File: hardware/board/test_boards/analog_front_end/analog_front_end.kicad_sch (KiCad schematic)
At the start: 13 parts, among them J1 Conn_01x20_Female, J2 Conn_01x20_Female, U6 LM27762

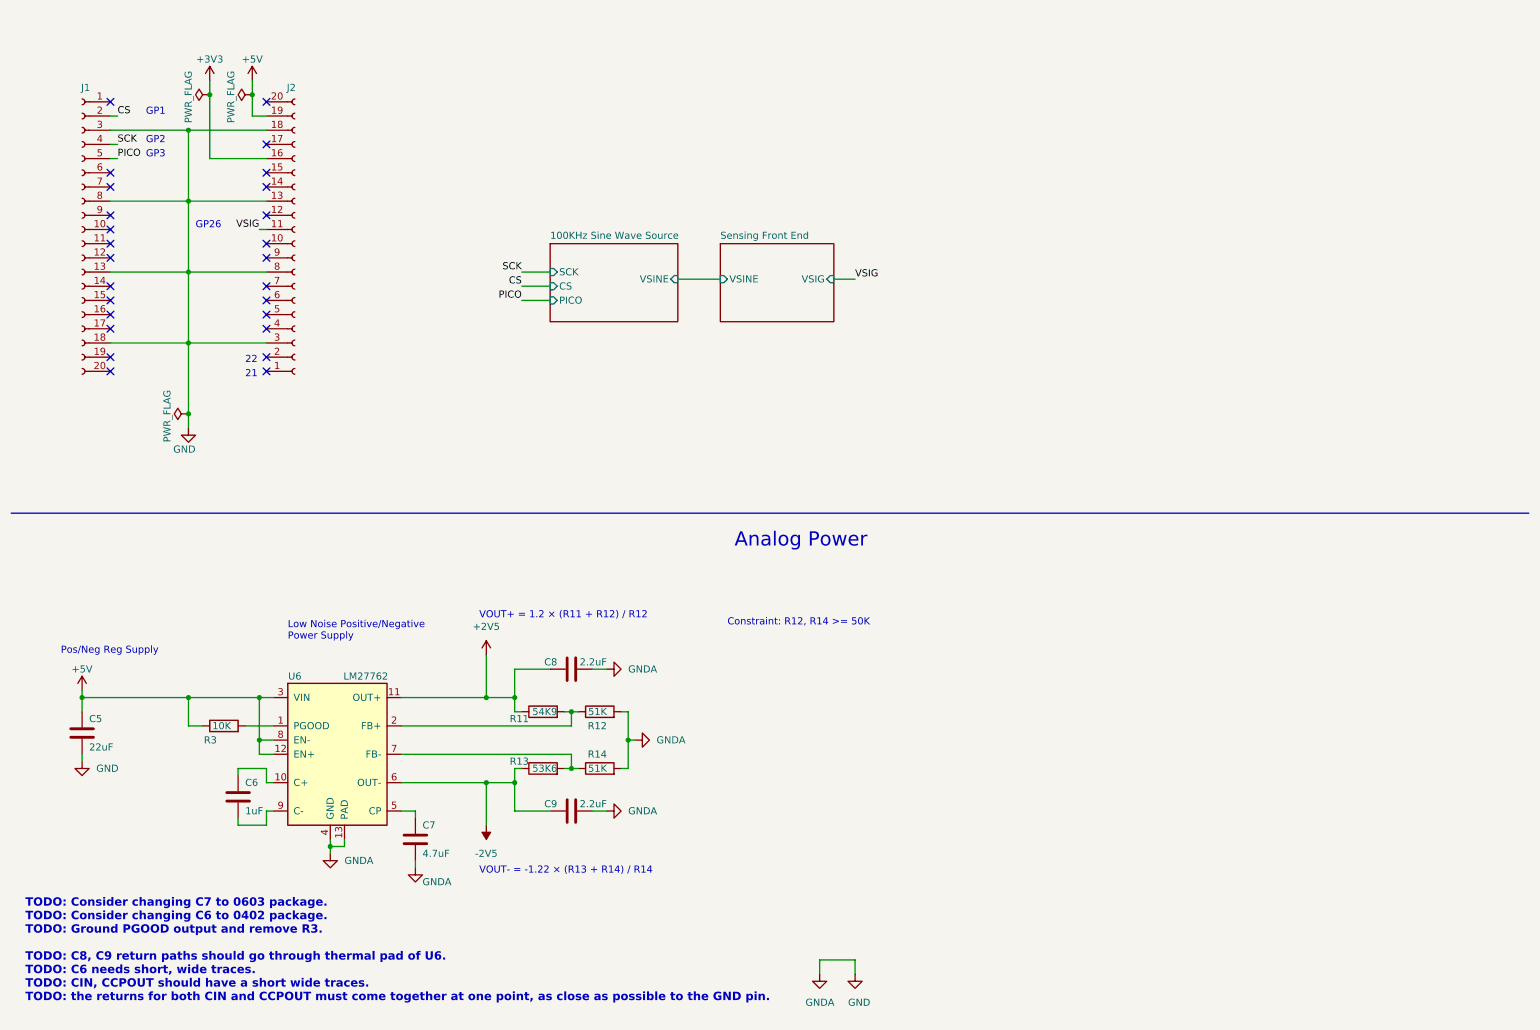
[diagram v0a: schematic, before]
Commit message: pcb rev3 with pcb guard and cable shield guard option
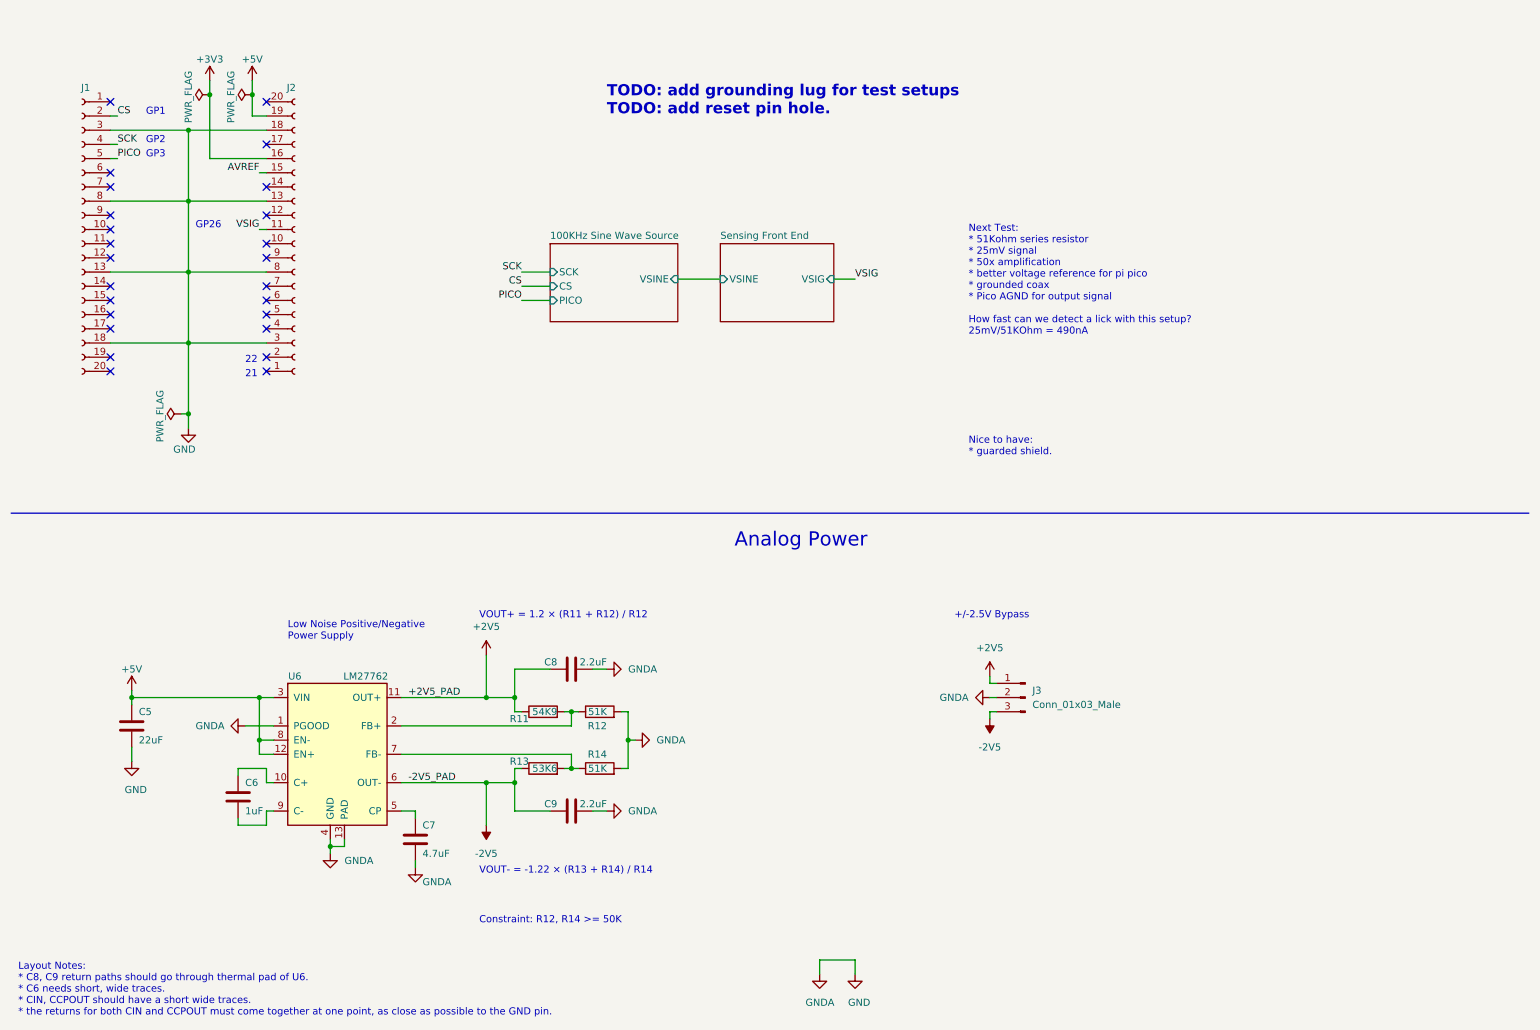
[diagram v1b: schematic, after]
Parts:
- removed R3: 10K, Resistor_SMD:R_0402_1005Metric_Pad0.72x0.64mm_HandSolder, symbol Device:R
- added J3: Conn_01x03_Male, Connector_PinHeader_2.54mm:PinHeader_1x03_P2.54mm_Vertical, symbol Connector:Conn_01x03_Male
- C6: footprint Capacitor_SMD:C_0603_1608Metric_Pad1.08x0.95mm_HandSolder -> Capacitor_SMD:C_0402_1005Metric_Pad0.74x0.62mm_HandSolder; Link https://www.digikey.com/en/products/detail/samsung-electro-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 -> https://www.digikey.com/en/products/detail/murata-electroni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; Manufacturer Samsung Electro-Mechanics -> Murata Electronics; Manufacturer Number CL10B105KA8NNNC -> GRM155R6YA105KE11J; Rated Voltage 25V -> 35V; Temperature Coefficient X7R -> X5R
- C7: footprint Capacitor_SMD:C_0805_2012Metric_Pad1.18x1.45mm_HandSolder -> Capacitor_SMD:C_0603_1608Metric_Pad1.08x0.95mm_HandSolder; Link https://www.digikey.com/en/products/detail/murata-electroni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 -> https://www.digikey.com/en/products/detail/samsung-electro-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; Manufacturer Murata Electronics -> Samsung Electro-Mechanics; Manufacturer Number GRM21BZ71H475KE15K -> CL10A475MA8NQNC; Rated Voltage 50V -> 25V; Temperature Coefficient X7R -> X5R; Tolerance 10% -> 20%
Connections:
- net +2V5: now also J3.1 (Pin_1)
- net -2V5: now also J3.3 (Pin_3)
- net GND: now also U6.1 (PGOOD), J3.2 (Pin_2)
- net AVREF: now reaches J2.15 (Pin_15)
- no-connect marks 26 -> 25
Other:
- note added: "+/-2.5V Bypass"
- note added: "Layout Notes: * C8, C9 return paths should go through thermal pad of U6. * C6 needs short, wide traces. * CIN, CCPOUT should have a short wide traces. * the returns for both CIN and CCPOUT must come together at one point, as close as possible to the GND pin."
- note added: "Next Test: * 51Kohm series resistor * 25mV signal * 50x amplification * better voltage reference for pi pico * grounded coax * Pico AGND for output signal How fast can we detect a lick with this setup? 25mV/51KOhm = 490nA"
- note added: "Nice to have: * guarded shield."
- note added: "TODO: add grounding lug for test setups TODO: add reset pin hole."
- note removed: "Pos/Neg Reg Supply"
- note removed: "TODO: Consider changing C7 to 0603 package. TODO: Consider changing C6 to 0402 package. TODO: Ground PGOOD output and remove R3. TODO: C8, C9 return paths should go through thermal pad of U6. TODO: C6 needs short, wide traces. TODO: CIN, CCPOUT should have a short wide traces. TODO: the returns for both CIN and CCPOUT must come together at one point, as close as possible to the GND pin."
- moved on the sheet: C5

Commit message: add design notes
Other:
- note added: "Next Test: * 50Kohm series resistor (or 100K) * 25mV signal * 50x amplification * better voltage reference for pi pico * grounded coax * Pico AGND for output signal How fast can we detect a lick with this setup? 25mV/51KOhm = 490nA 25mV/100KOhm = 250nA"
- note removed: "Next Test: * 51Kohm series resistor * 25mV signal * 50x amplification * better voltage reference for pi pico * grounded coax * Pico AGND for output signal How fast can we detect a lick with this setup? 25mV/51KOhm = 490nA"
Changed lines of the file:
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@@
     (effects (font (size 1.27 1.27)) (justify left bottom))
   )
-  (text "Next Test:\n* 51Kohm series resistor\n* 25mV signal\n* 50x amplification\n* better voltage reference for pi pico\n* grounded coax\n* Pico AGND for output signal\n\nHow fast can we detect a lick with this setup?\n25mV/51KOhm = 490nA"
+  (text "Next Test:\n* 50Kohm series resistor (or 100K)\n* 25mV signal\n* 50x amplification\n* better voltage reference for pi pico\n* grounded coax\n* Pico AGND for output signal\n\nHow fast can we detect a lick with this setup?\n25mV/51KOhm = 490nA\n25mV/100KOhm = 250nA"
     (at 184.15 73.66 0)
     (effects (font (size 1.27 1.27)) (justify left bottom))
@@
     )
     (path "/8ca25f6d-cadc-4d60-beba-2de6b7c14b93/bd724835-3e3e-41a0-bd03-a1c31e2ef475"
-      (reference "R23") (unit 1) (value "50K") (footprint "Resistor_SMD:R_1206_3216Metric")
+      (reference "R23") (unit 1) (value "100K") (footprint "Resistor_SMD:R_1206_3216Metric")
     )
     (path "/82c6d2bc-a975-44eb-8d35-610dba9024de/5e7ff8f9-784d-4070-ab43-581307fcfb6d"

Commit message: update bom
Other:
- note added: "Bringup Test Config 1: * 50Kohm series resistor (or 100K) * 25mV signal * 50x total amplification * guarded coax Bringup Test Config 2: * 50Kohm series resistor (or 100K) * 25mV signal * 50x total amplification * grounded coax Bringup Test Config 3: * 50Kohm series resistor (or 100K) * 25mV signal * 50x total amplification * coax with floating shield Bringup Test Config 4: * 1Mohm series resistor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"
- note added: "TODO: add reset pin hole."
- note removed: "Next Test: * 50Kohm series resistor (or 100K) * 25mV signal * 50x amplification * better voltage reference for pi pico * grounded coax * Pico AGND for output signal How fast can we detect a lick with this setup? 25mV/51KOhm = 490nA 25mV/100KOhm = 250nA"
- note removed: "Nice to have: * guarded shield."
- note removed: "TODO: add grounding lug for test setups TODO: add reset pin hole."

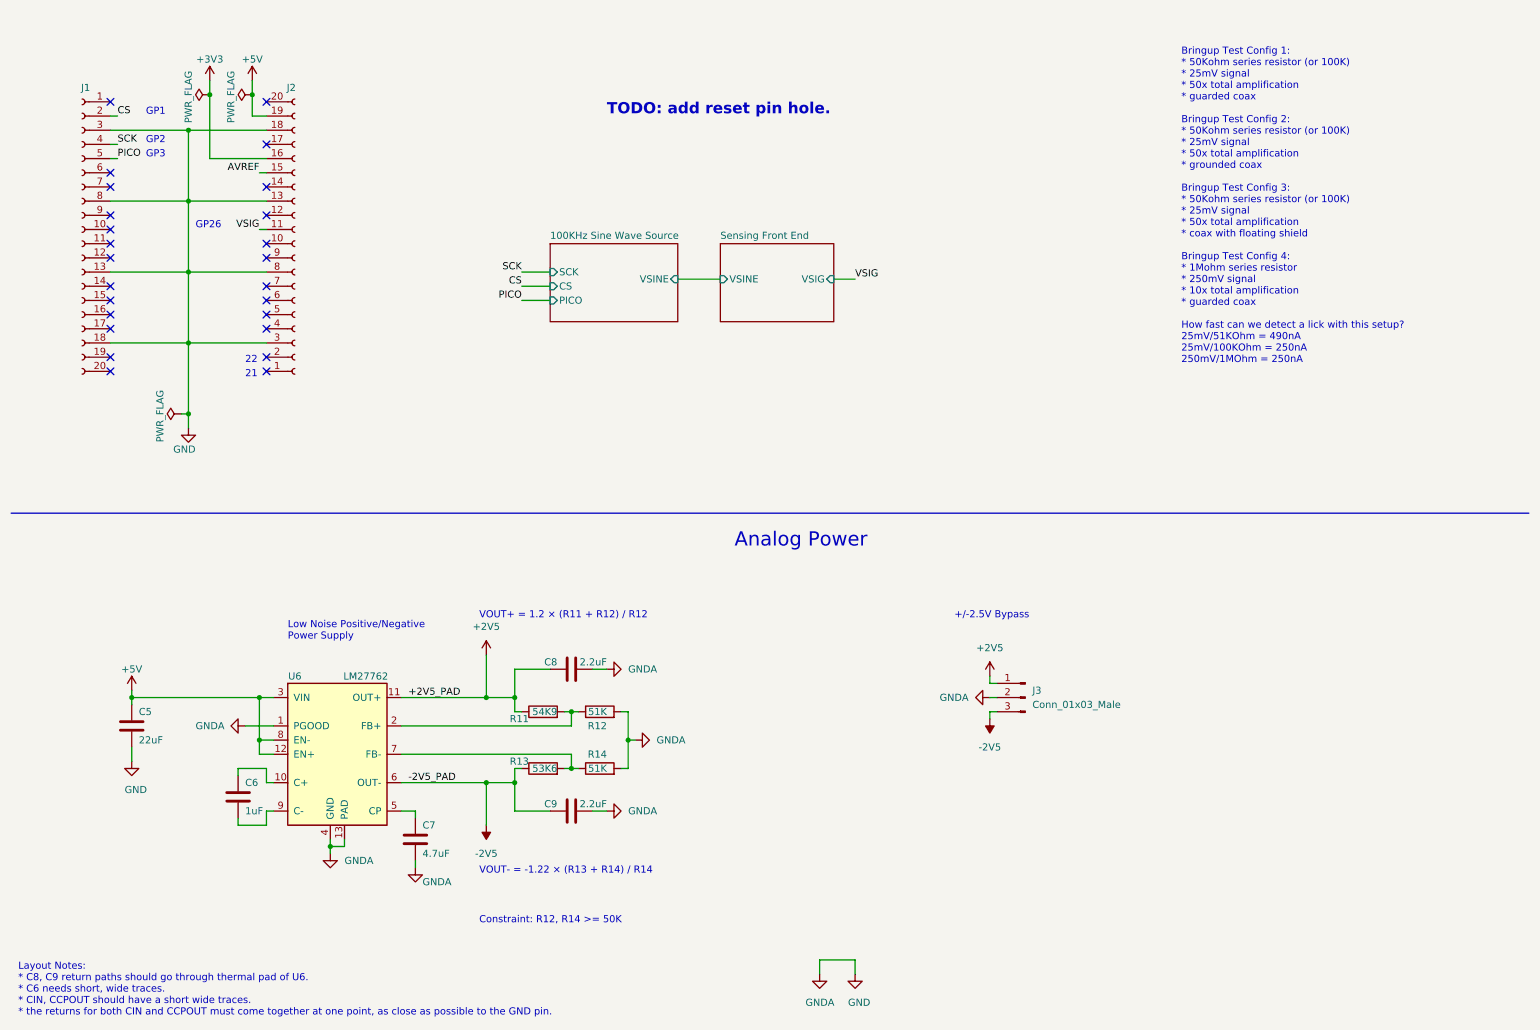
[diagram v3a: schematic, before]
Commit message: layout rev4 with triax and ltc6269
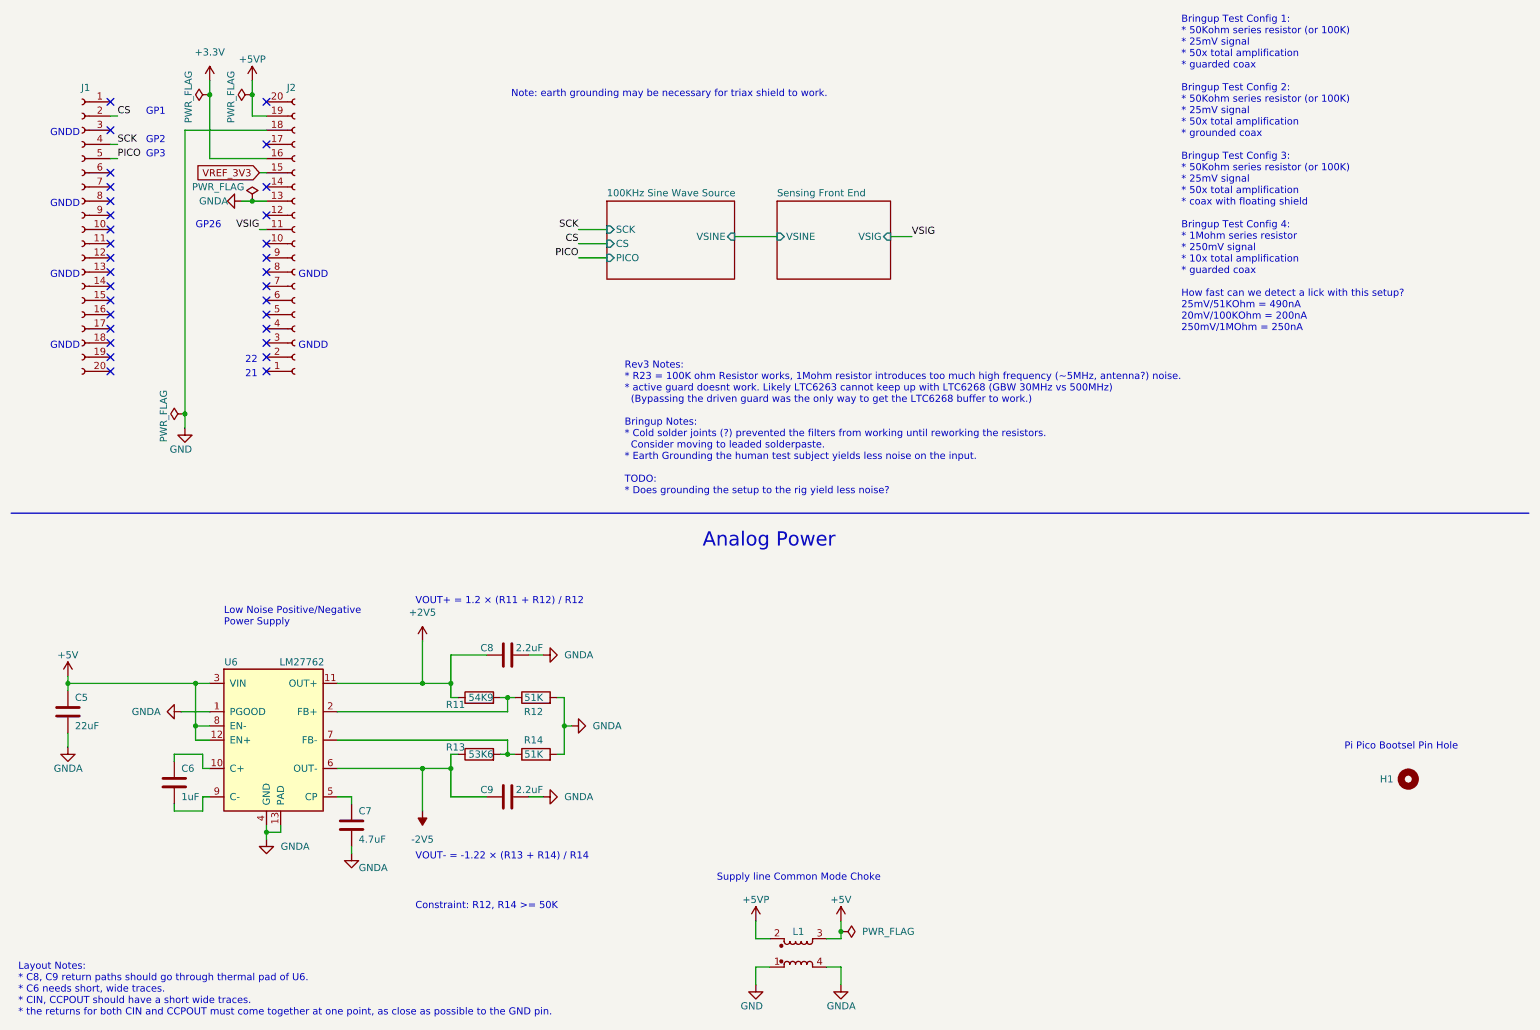
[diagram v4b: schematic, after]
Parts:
- removed J3: Conn_01x03_Male, Connector_PinHeader_2.54mm:PinHeader_1x03_P2.54mm_Vertical, symbol Connector:Conn_01x03_Male
- added H1: MountingHole, MountingHole:MountingHole_2.2mm_M2_DIN965, symbol Mechanical:MountingHole
- added L1: L_Coupled_1423, kicad_component_library:L_CommonModeChoke_TDKCorporation_1210, symbol Device:L_Coupled_1423
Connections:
- net +5V: now also L1.3; no longer J2.19 (Pin_19)
- net GND: now also L1.1; no longer C5.2, C7.2, C8.2, C9.2, J1.13 (Pin_13), J1.18 (Pin_18), J1.3 (Pin_3), J1.8 (Pin_8), J2.13 (Pin_13), J2.3 (Pin_3), J2.8 (Pin_8), R12.2, R14.2, U6.1 (PGOOD), U6.13 (PAD), U6.4 (GND)
- net AVREF renamed VREF_3V3
- new net +5VP: J2.19 (Pin_19), L1.2
- new net GNDA: C5.2, C7.2, C8.2, C9.2, J2.13 (Pin_13), L1.4, R12.2, R14.2, U6.1 (PGOOD), U6.13 (PAD), U6.4 (GND)
- no-connect marks 25 -> 31
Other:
- note added: "GNDD"
- note added: "Note: earth grounding may be necessary for triax shield to work."
- note added: "Pi Pico Bootsel Pin Hole"
- note added: "Rev3 Notes: * R23 = 100K ohm Resistor works, 1Mohm resistor introduces too much high frequency (~5MHz, antenna?) noise. * active guard doesnt work. Likely LTC6263 cannot keep up with LTC6268 (GBW 30MHz vs 500MHz) (Bypassing the driven guard was the only way to get the LTC6268 buffer to work.) Bringup Notes: * Cold solder joints (?) prevented the filters from working until reworking the resistors.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"
- note added: "Supply line Common Mode Choke"
- note removed: "+/-2.5V Bypass"
- note removed: "TODO: add reset pin hole."
- moved on the sheet: C5, C6, C7, C8, C9, R11, R12, R13, R14, U6

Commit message: update bom
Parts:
- H1: Link (none) -> n/a; Manufacturer (none) -> n/a; Manufacturer Number (none) -> n/a
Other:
- note removed: "Bringup Test Config 1: * 50Kohm series resistor (or 100K) * 25mV signal * 50x total amplification * guarded coax Bringup Test Config 2: * 50Kohm series resistor (or 100K) * 25mV signal * 50x total amplification * grounded coax Bringup Test Config 3: * 50Kohm series resistor (or 100K) * 25mV signal * 50x total amplification * coax with floating shield Bringup Test Config 4: * 1Mohm series resistor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"
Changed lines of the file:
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@@
-    (effects (font (size 1.27 1.27)) (justify left bottom))
-  )
-  (text "Bringup Test Config 1:\n* 50Kohm series resistor (or 100K)\n* 25mV signal\n* 50x total amplification\n* guarded coax\n\nBringup Test Config 2:\n* 50Kohm series resistor (or 100K)\n* 25mV signal\n* 50x total amplification\n* grounded coax\n\nBringup Test Config 3:\n* 50Kohm series resistor (or 100K)\n* 25mV signal\n* 50x total amplification\n* coax with floating shield\n\nBringup Test Config 4:\n* 1Mohm series resistor\n* 250mV signal\n* 10x total amplification\n* guarded coax\n\nHow fast can we detect a lick with this setup?\n25mV/51KOhm = 490nA\n20mV/100KOhm = 200nA\n250mV/1MOhm = 250nA"
-    (at 222.25 73.025 0)
     (effects (font (size 1.27 1.27)) (justify left bottom))
   )
@@
       (effects (font (size 1.27 1.27)) hide)
     )
-    (property "Datasheet" "~" (at 262.89 153.035 0)
-      (effects (font (size 1.27 1.27)) hide)
-    )
+    (property "Datasheet" "n/a" (at 262.89 153.035 0)
+      (effects (font (size 1.27 1.27)) hide)
+    )
+    (property "Link" "n/a" (at 262.89 153.035 0)
+      (effects (font (size 1.27 1.27)) hide)
+    )
+    (property "Manufacturer" "n/a" (at 262.89 153.035 0)
+      (effects (font (size 1.27 1.27)) hide)
+    )
+    (property "Manufacturer Number" "n/a" (at 262.89 153.035 0)
+      (effects (font (size 1.27 1.27)) hide)
+    )
